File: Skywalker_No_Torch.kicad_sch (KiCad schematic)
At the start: 37 parts

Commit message: no message
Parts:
- removed 3WayPBall?: ~, symbol PID_symbols:3WayPmaticBall
- added 3WayPBall1: ~, symbol PID_symbols:3WayPmaticBall
- added Stop1: ~, symbol PID_symbols:Stop
- gave numbers to parts that had none: 36
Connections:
- net ATM: now also 3WayPBall1. (IN/OUT)
- net at N1.: now also CV1., N2_Hose1., Reg1., Reg2.
- net at Engine1.: now also Fuel_Inj1.; no longer Ox_Inj1.
- net at Fuel_Inj1.: no longer Engine1.
- net at Pn_Sol1.: now also 3WayPBall1. (IN/OUT)
- net at CV4.: now also Stop1.; no longer Ox1.
- net at Hose2.1: now also 3WayPBall1. (IN/OUT)
- new net: Engine1., Ox_Inj1.
- new net: Fuel1., Hose1.1, MB_V1.
- new net: Burst_Disc1., CV2., Fuel1., PT2., SPRV1., nO_Sol4.
- new net: BV1., CV2., CV3.
- new net: PT3., Pn_Sol1., Reg1., nO_Sol1., nO_Sol2.
- new net: BV2., Burst_Disc2., CV3., Ox1., PT1., SPRV2.
- new net: CV4., QD2.
- new net: 3WayPBall1. (IN/OUT), Ox1., Stop1.
- now unconnected: BV3., Burst_Disc1., Burst_Disc2., N2_Hose1., PT1., PT2., PT3.
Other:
- moved on the sheet: BV3, BV4, Chamber1, Engine1, Fuel_Inj1, Hose1, Hose2, Ox_Inj1

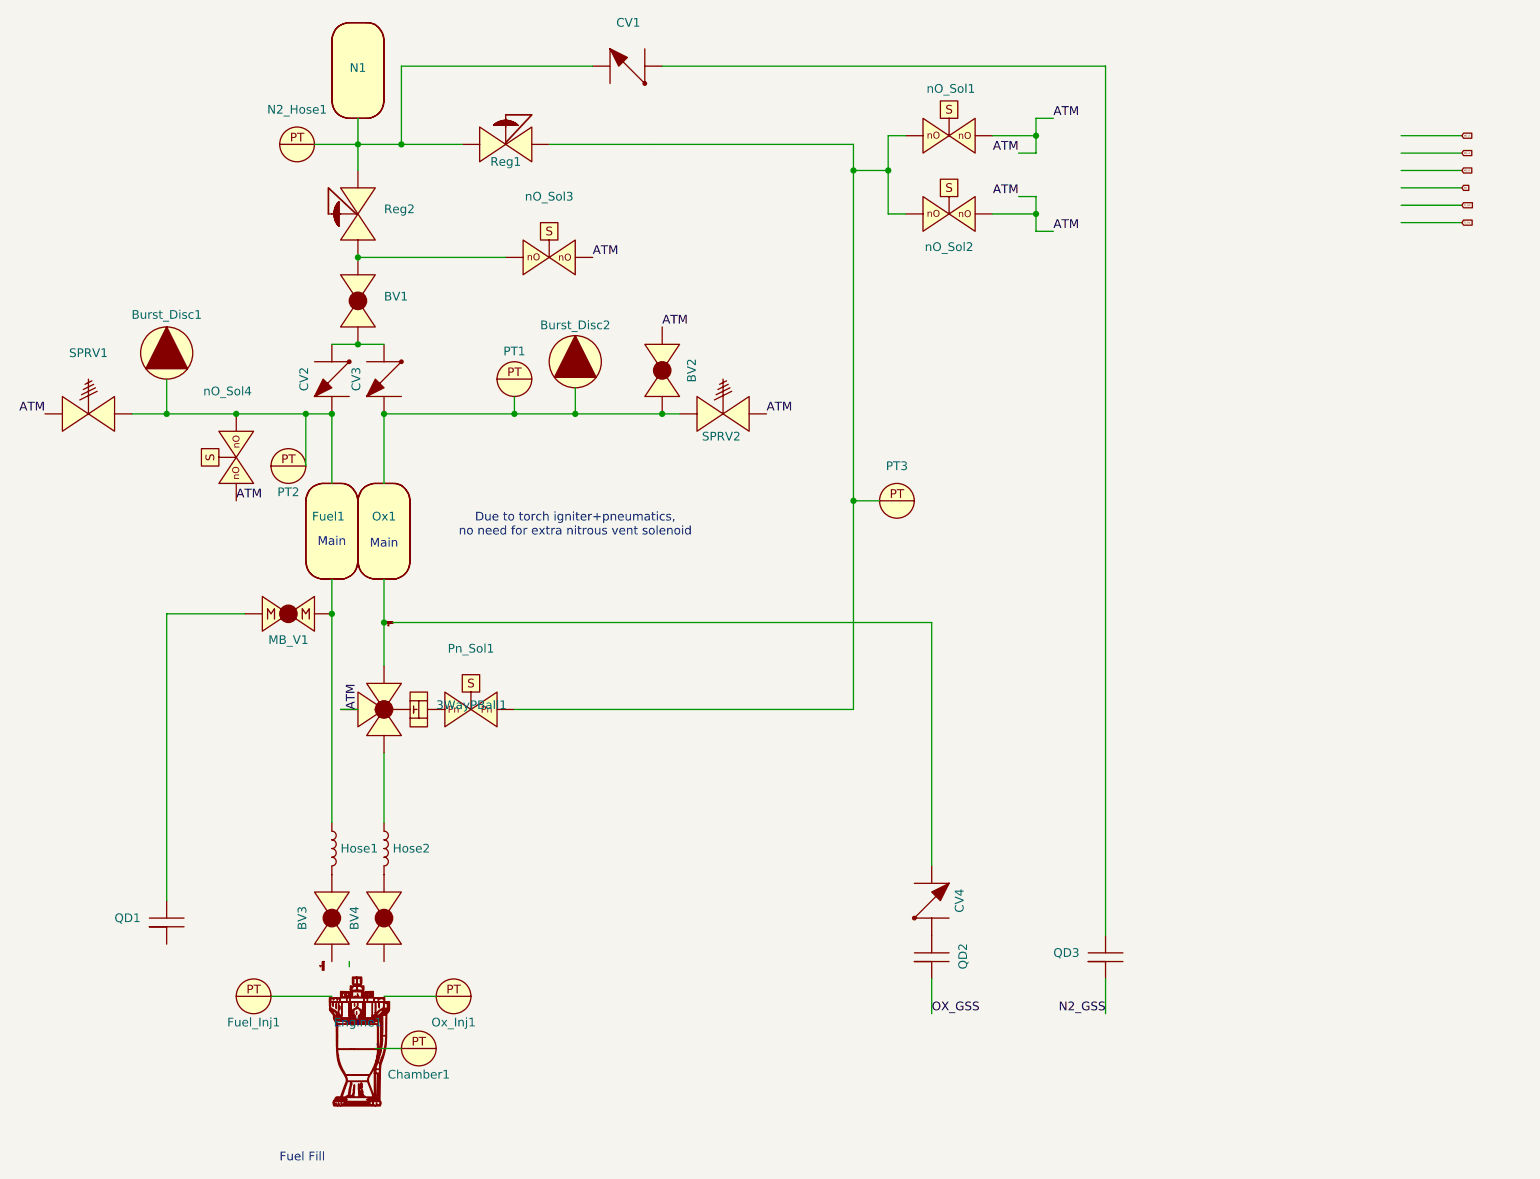
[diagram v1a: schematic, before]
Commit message: added universal key
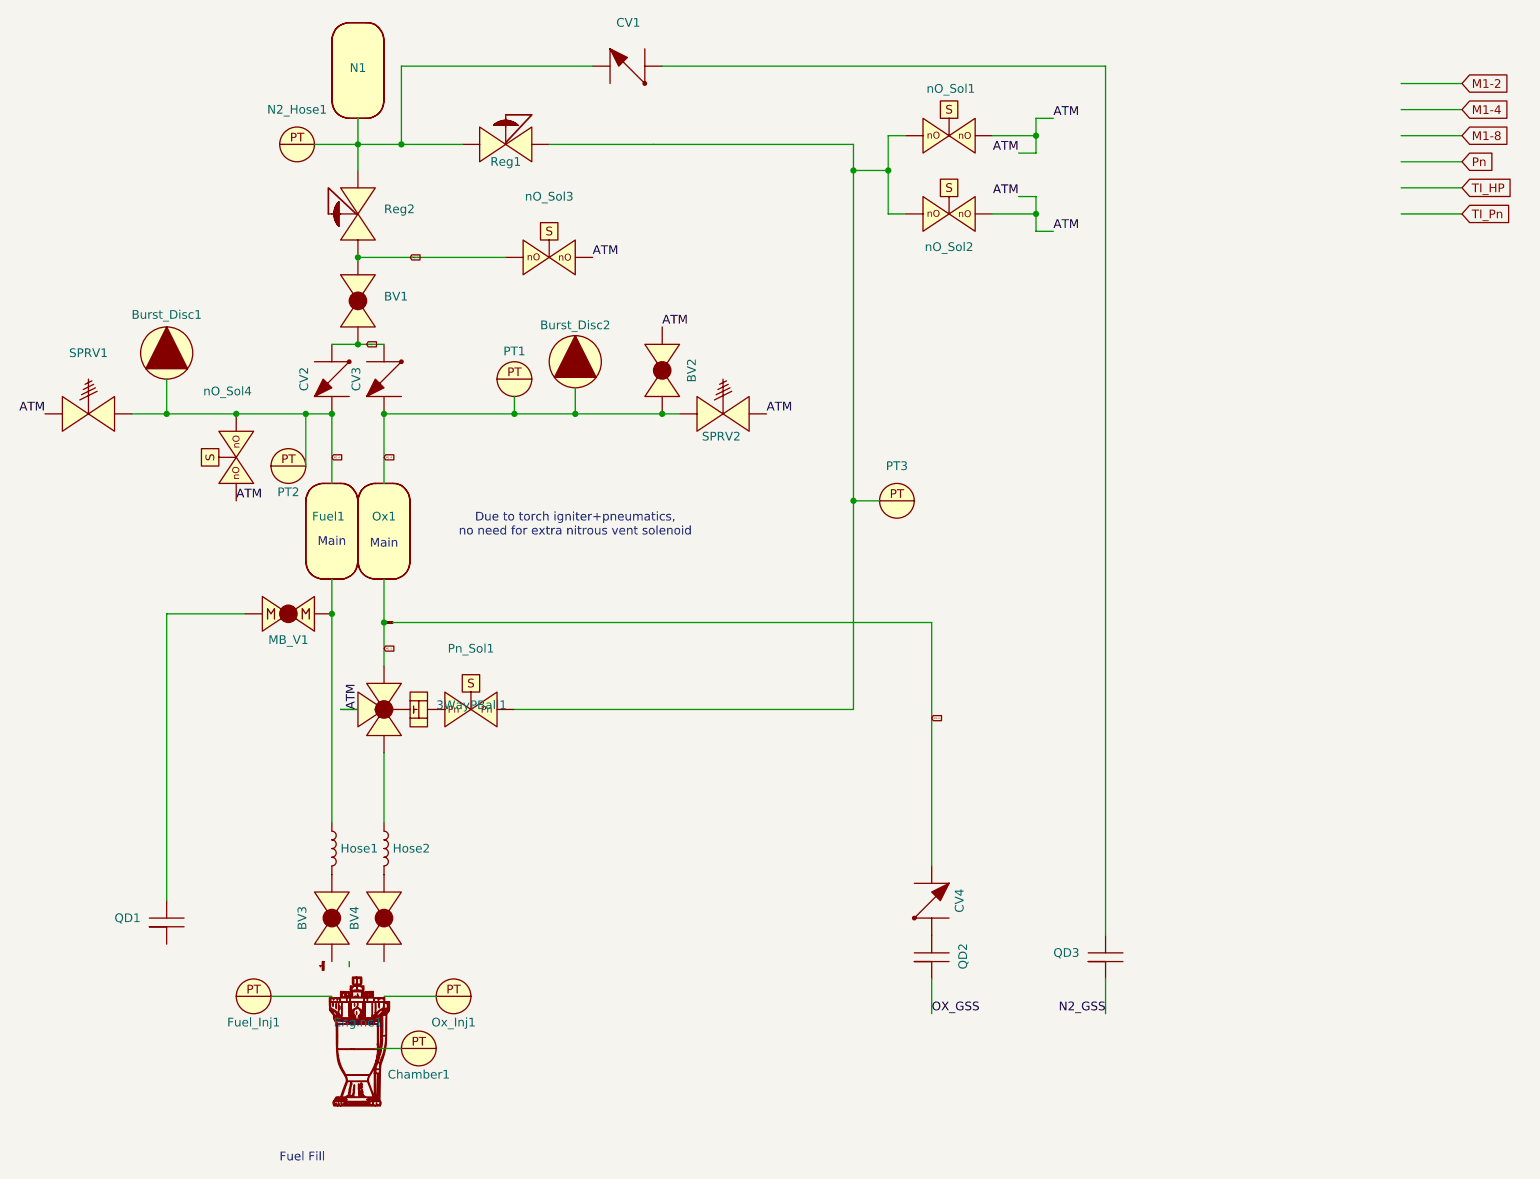
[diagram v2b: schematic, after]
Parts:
- removed unit 1 of Stop1
- added U1: ~, symbol PID_symbols:stop
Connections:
- net M1-2: now also 3WayPBall1., Ox1., U1.
- net M1-4: now also BV1., BV2., Burst_Disc1., Burst_Disc2., CV2., CV3., CV4., Fuel1., Ox1., PT1., PT2., Reg2., SPRV1., SPRV2., nO_Sol3., nO_Sol4., U1.
- net at N1.: now also CV1., N2_Hose1., Reg1., Reg2.
- net at Engine1.: now also Fuel_Inj1.
- net at Ox_Inj1.: no longer Engine1.
- net at Fuel_Inj1.: no longer Engine1.
- net at BV4.: now also Hose2.2
- new net: Engine1., Ox_Inj1.
- new net: Fuel1., Hose1.1, MB_V1.
- new net: PT3., Pn_Sol1., Reg1., nO_Sol1., nO_Sol2.
- new net: CV4., QD2.
- now unconnected: N2_Hose1., PT3.

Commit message: no message
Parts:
- removed Stop1: ~, symbol PID_symbols:Stop
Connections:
- net . is gone; now on net D: Chamber1.
- net ATM: no longer nO_Sol1., nO_Sol2.
- net M1-2: no longer 3WayPBall1., Ox1., U1.
- net Pn: now also PT3., Pn_Sol1., Reg1., nO_Sol1., nO_Sol2.
- net 1-4: now reaches N1.
- net 1-4: now also BV1., BV2., BV3., BV4., Burst_Disc1., Burst_Disc2., CV1., CV2., CV3., CV4., Engine1., Fuel1., Hose1.1, MB_V1., N2_Hose1., Ox1., PT1., PT2., QD1., QD3., Reg1., Reg2., SPRV1., SPRV2., U1., nO_Sol3., nO_Sol4.
- net D: now reaches Chamber1.
- net D: now also Engine1., Fuel_Inj1., Ox_Inj1.
- net 1-2: now reaches 3WayPBall1., Hose2.1
- net 1-2: now also Ox1., U1.
- removed net M1-4: BV1., BV2., Burst_Disc1., Burst_Disc2., CV2., CV3., CV4., Fuel1., Ox1., PT1., PT2., Reg2., SPRV1., SPRV2., U1., nO_Sol3., nO_Sol4.
- new net: BV1., CV2., CV3.
- new net: CV4., QD2.
- new net: 3WayPBall1., Pn_Sol1.

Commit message: cleanup cos i was bored and procastinating. mini tutorial on defining pipe sizes in the p&id.
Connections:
- new net: BV1., CV2., CV3.
- new net: CV4., QD2.
- new net: 3WayPBall1., Pn_Sol1.

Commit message: bored
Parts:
- added U10, U7, U8, U9: ~, symbol PID_symbols:stop
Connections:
- net ATM: now also U10., U7., U8., U9.
- net OX_GSS: now also QD1.
- net Pn: now also U10., U7., U8., U9.
- new net: BV1., CV2., CV3.
- new net: CV4., QD2.
- new net: 3WayPBall1., Pn_Sol1.
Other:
- moved on the sheet: QD3
